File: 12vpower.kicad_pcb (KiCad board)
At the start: 2 copper layers, 63.2 x 41.9 mm, 23 parts, among them J1 Conn_02x08_Odd_Even, J2 Conn_02x08_Odd_Even, J3 Conn_02x08_Odd_Even, P1 15 in, P2 12, P3 12, U1 L7812, U2 L7912, U3 L7805

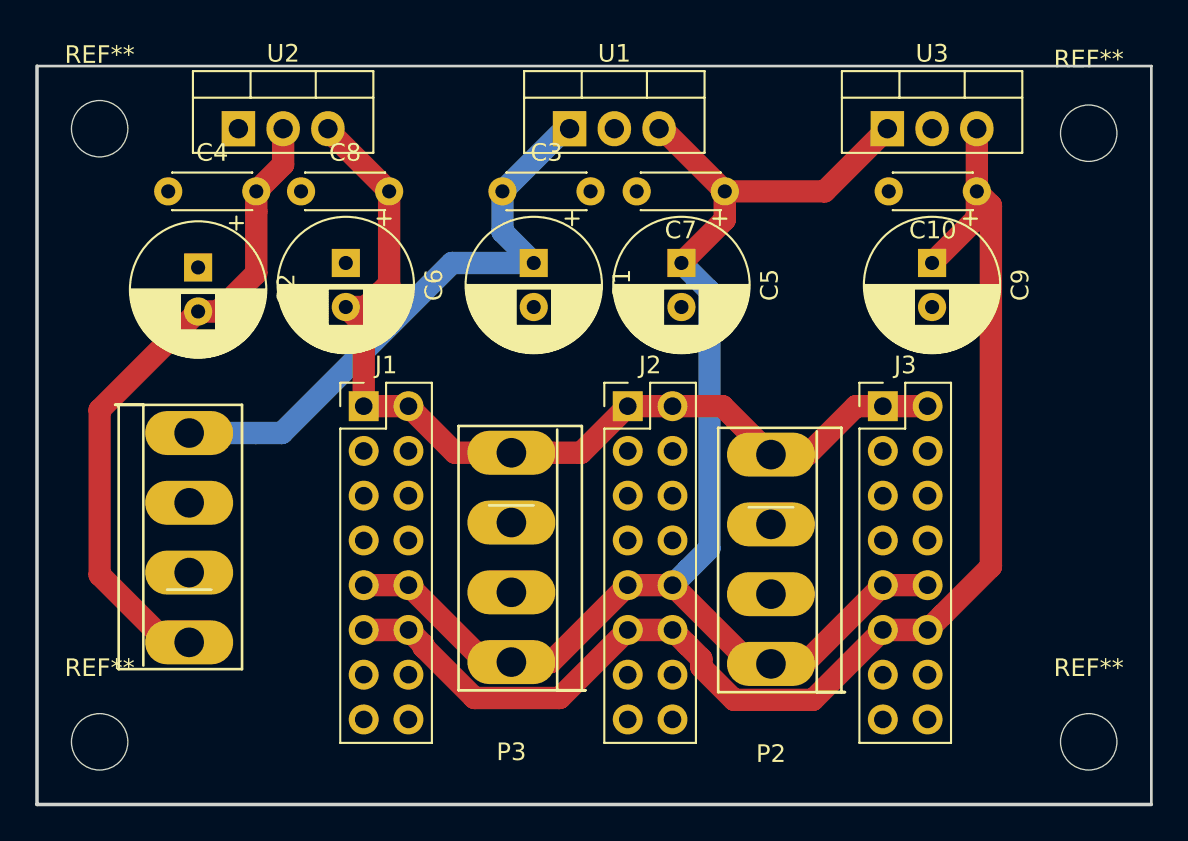
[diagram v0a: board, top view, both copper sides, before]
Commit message: moved a few things around, updated labels
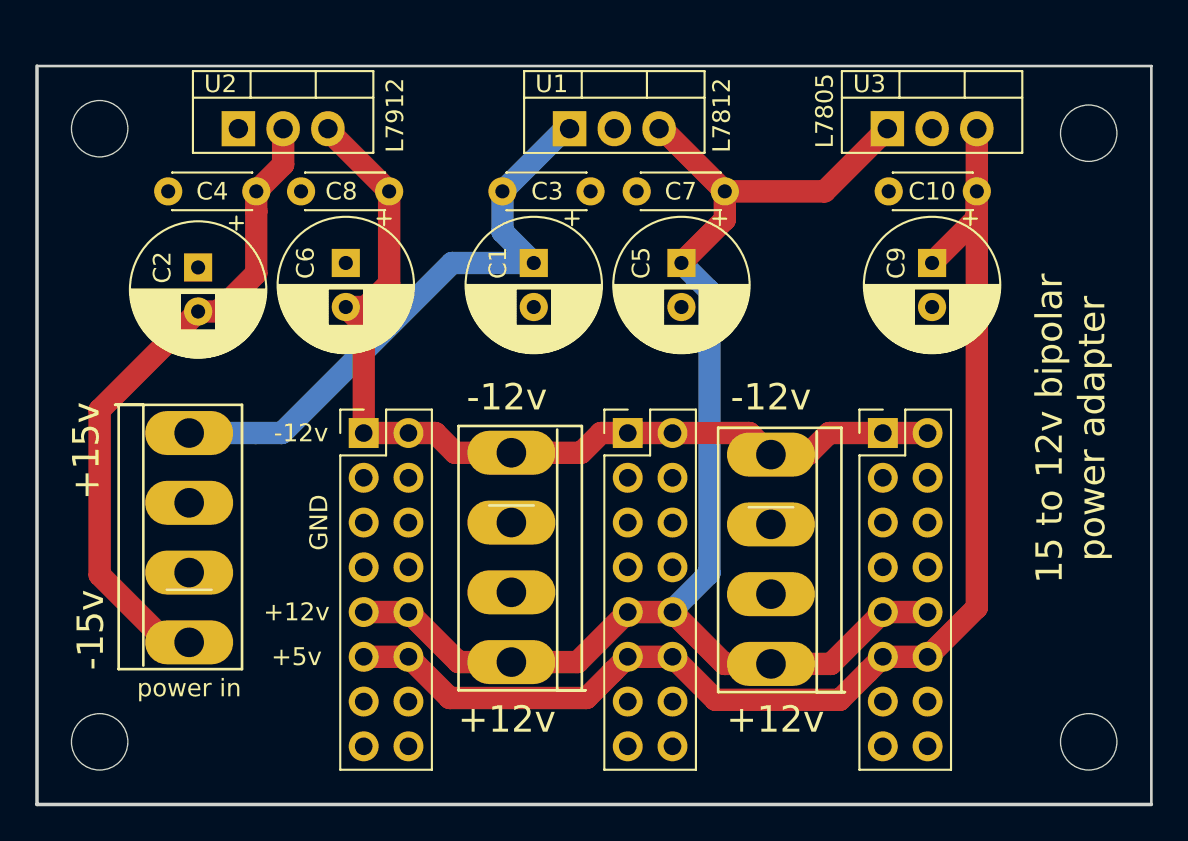
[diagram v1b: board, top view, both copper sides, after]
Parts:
- P1: value 15 in -> power in
- moved J1 1.52 mm to (43.2, 102.1)
- moved J2 1.52 mm to (58.2, 102.1)
- moved J3 1.52 mm to (72.6, 102.1)
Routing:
- net +5V: track 74.2 -> 72.2 mm
- net -12V: track 55.8 -> 54.8 mm
- net +12V: track 80.1 -> 79.1 mm
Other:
- board text added: "+12v"
- board text added: "+15v"
- board text added: "+5v"
- board text added: "-12v"
- board text added: "-15v"
- board text added: "15 to 12v bipolar power adapter"
- board text added: "GND"

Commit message: label movement
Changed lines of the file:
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@@
   )
   (setup
-    (last_trace_width 1.27)
+    (last_trace_width 0.1524)
     (user_trace_width 0.254)
     (user_trace_width 0.635)
@@
       (effects (font (size 1 1) (thickness 0.15)))
     )
-    (fp_text value L7812 (at 8.636 -0.762 90) (layer F.SilkS)
+    (fp_text value L7812 (at -3.556 -0.762 90) (layer F.SilkS)
       (effects (font (size 1 1) (thickness 0.15)))
     )
@@
       (effects (font (size 1 1) (thickness 0.15)))
     )
-    (fp_text value L7912 (at 8.89 -0.762 90) (layer F.SilkS)
+    (fp_text value L7912 (at -3.556 -0.762 90) (layer F.SilkS)
       (effects (font (size 1 1) (thickness 0.15)))
     )
@@
       (effects (font (size 1 1) (thickness 0.15)))
     )
-    (fp_text value L7805 (at -3.556 -1.016 90) (layer F.SilkS)
-      (effects (font (size 1 1) (thickness 0.15)))
-    )
+    (fp_text value L7805 (at -3.556 -0.762 90) (layer F.SilkS)
+      (effects (font (size 1 1) (thickness 0.15)))
+    )
